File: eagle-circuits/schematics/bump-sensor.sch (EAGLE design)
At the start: 6 parts, among them J1 ARDUINO_uno

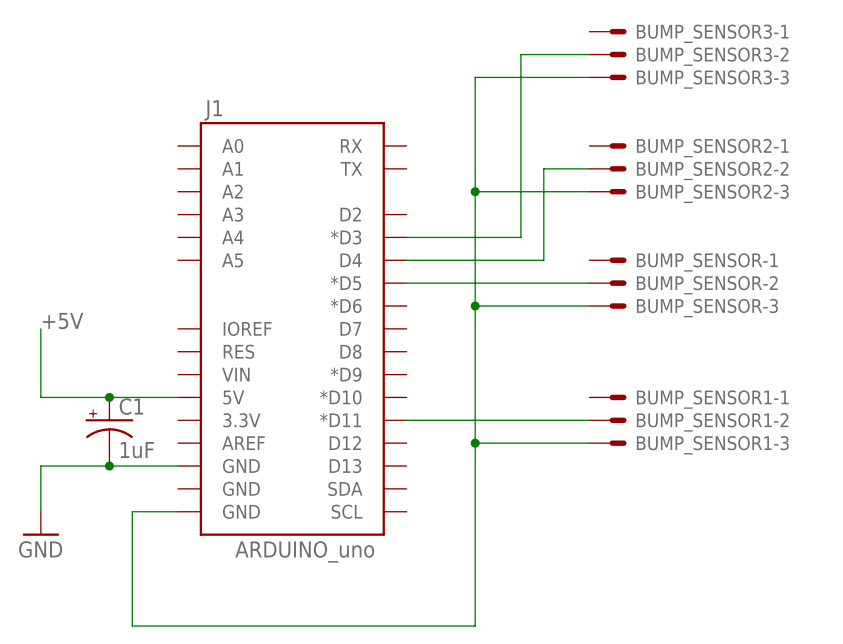
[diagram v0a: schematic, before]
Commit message: updated eagle schematic for bumper
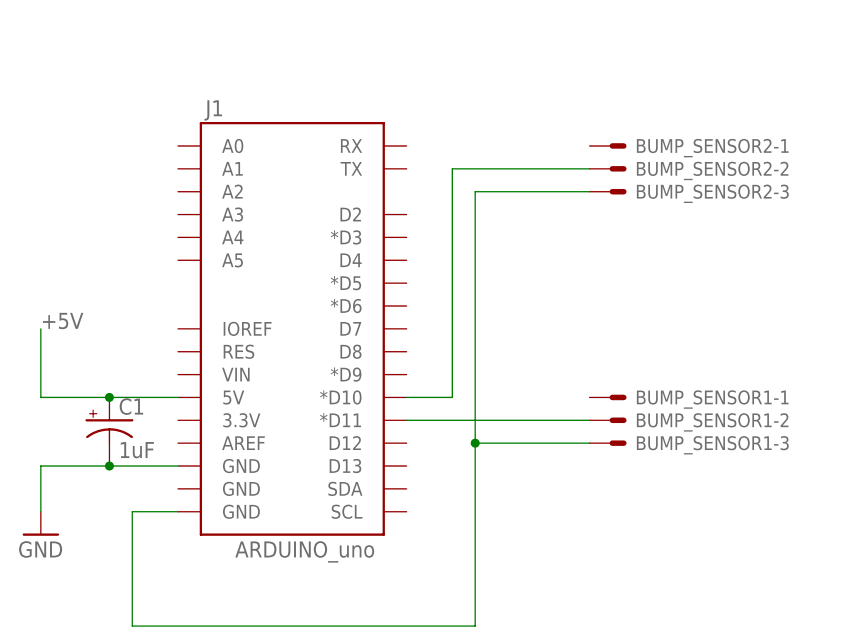
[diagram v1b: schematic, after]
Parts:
- removed BUMP_SENSOR, BUMP_SENSOR3: 22-23-2031, con-molex:22-23-2031
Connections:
- removed net N$6: BUMP_SENSOR2-2.S, J1.D4
- removed net N$7: BUMP_SENSOR3-2.S, J1.*D3
- net N$2: now also BUMP_SENSOR2-2.S, J1.*D10; no longer BUMP_SENSOR-2.S, J1.*D5
- net N$3: no longer BUMP_SENSOR-3.S, BUMP_SENSOR3-3.S
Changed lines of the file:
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@@
 <parts>
 <part name="FRAME1" library="frames" deviceset="A4L-LOC" device=""/>
-<part name="BUMP_SENSOR" library="con-molex" deviceset="22-23-2031" device="" value=""/>
 <part name="J1" library="ME210Lib_2015_v2" deviceset="ARDUINO_R3_SHIELD" device="" value="ARDUINO_uno"/>
 <part name="C1" library="ME210Lib_2015_v2" deviceset="CAP_POL" device="1206" value="1uF"/>
@@
 <part name="BUMP_SENSOR1" library="con-molex" deviceset="22-23-2031" device="" value=""/>
 <part name="BUMP_SENSOR2" library="con-molex" deviceset="22-23-2031" device="" value=""/>
-<part name="BUMP_SENSOR3" library="con-molex" deviceset="22-23-2031" device="" value=""/>
 </parts>
 <sheets>
@@
 <instances>
 <instance part="FRAME1" gate="G$1" x="0" y="0"/>
-<instance part="BUMP_SENSOR" gate="-1" x="160.02" y="104.14"/>
-<instance part="BUMP_SENSOR" gate="-2" x="160.02" y="101.6"/>
-<instance part="BUMP_SENSOR" gate="-3" x="160.02" y="99.06"/>
 <instance part="J1" gate="G$1" x="124.46" y="99.06"/>
 <instance part="C1" gate="G$1" x="104.14" y="86.36"/>
@@
 <instance part="BUMP_SENSOR2" gate="-2" x="160.02" y="114.3"/>
 <instance part="BUMP_SENSOR2" gate="-3" x="160.02" y="111.76"/>
-<instance part="BUMP_SENSOR3" gate="-1" x="160.02" y="129.54"/>
-<instance part="BUMP_SENSOR3" gate="-2" x="160.02" y="127"/>
-<instance part="BUMP_SENSOR3" gate="-3" x="160.02" y="124.46"/>
 </instances>
 <busses>
@@
 <net name="N$3" class="0">
 <segment>
-<pinref part="BUMP_SENSOR" gate="-3" pin="S"/>
-<wire x1="157.48" y1="99.06" x2="144.78" y2="99.06" width="0.1524" layer="91"/>
-<wire x1="144.78" y1="99.06" x2="144.78" y2="83.82" width="0.1524" layer="91"/>
+<wire x1="144.78" y1="111.76" x2="144.78" y2="83.82" width="0.1524" layer="91"/>
 <wire x1="144.78" y1="83.82" x2="144.78" y2="63.5" width="0.1524" layer="91"/>
 <wire x1="144.78" y1="63.5" x2="106.68" y2="63.5" width="0.1524" layer="91"/>
@@
 <pinref part="BUMP_SENSOR2" gate="-3" pin="S"/>
 <wire x1="157.48" y1="111.76" x2="144.78" y2="111.76" width="0.1524" layer="91"/>
-<wire x1="144.78" y1="111.76" x2="144.78" y2="99.06" width="0.1524" layer="91"/>
-<junction x="144.78" y="99.06"/>
-<pinref part="BUMP_SENSOR3" gate="-3" pin="S"/>
-<wire x1="157.48" y1="124.46" x2="144.78" y2="124.46" width="0.1524" layer="91"/>
-<wire x1="144.78" y1="124.46" x2="144.78" y2="111.76" width="0.1524" layer="91"/>
-<junction x="144.78" y="111.76"/>
 </segment>
 </net>
@@
 <net name="N$2" class="0">
 <segment>
-<pinref part="BUMP_SENSOR" gate="-2" pin="S"/>
-<pinref part="J1" gate="G$1" pin="*D5"/>
-<wire x1="157.48" y1="101.6" x2="137.16" y2="101.6" width="0.1524" layer="91"/>
+<pinref part="BUMP_SENSOR2" gate="-2" pin="S"/>
+<wire x1="157.48" y1="114.3" x2="142.24" y2="114.3" width="0.1524" layer="91"/>
+<wire x1="142.24" y1="114.3" x2="142.24" y2="88.9" width="0.1524" layer="91"/>
+<pinref part="J1" gate="G$1" pin="*D10"/>
+<wire x1="142.24" y1="88.9" x2="137.16" y2="88.9" width="0.1524" layer="91"/>
 </segment>
 </net>
-<net name="N$6" class="0">
-<segment>
-<pinref part="BUMP_SENSOR2" gate="-2" pin="S"/>
-<wire x1="157.48" y1="114.3" x2="152.4" y2="114.3" width="0.1524" layer="91"/>
-<wire x1="152.4" y1="114.3" x2="152.4" y2="104.14" width="0.1524" layer="91"/>
-<pinref part="J1" gate="G$1" pin="D4"/>
-<wire x1="152.4" y1="104.14" x2="137.16" y2="104.14" width="0.1524" layer="91"/>
-</segment>
-</net>
-<net name="N$7" class="0">
-<segment>
-<pinref part="BUMP_SENSOR3" gate="-2" pin="S"/>
-<wire x1="157.48" y1="127" x2="149.86" y2="127" width="0.1524" layer="91"/>
-<wire x1="149.86" y1="127" x2="149.86" y2="106.68" width="0.1524" layer="91"/>
-<pinref part="J1" gate="G$1" pin="*D3"/>
-<wire x1="149.86" y1="106.68" x2="137.16" y2="106.68" width="0.1524" layer="91"/>
-</segment>
-</net>
